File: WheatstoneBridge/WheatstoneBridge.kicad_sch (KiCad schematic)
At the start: 6 parts

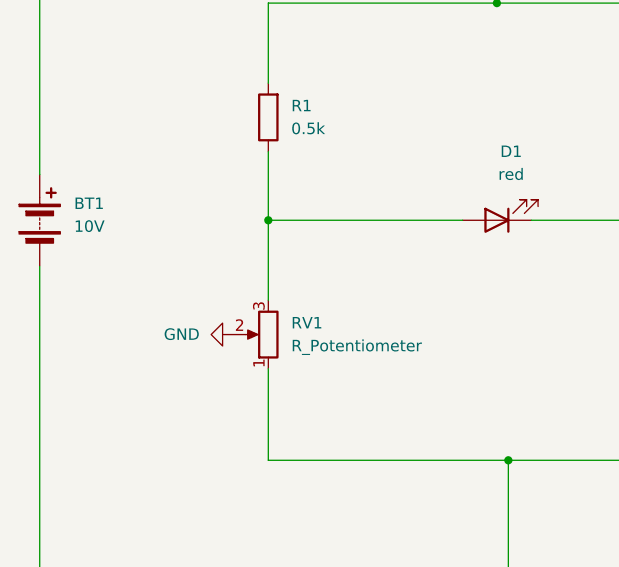
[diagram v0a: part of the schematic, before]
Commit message: Add 4bits adder
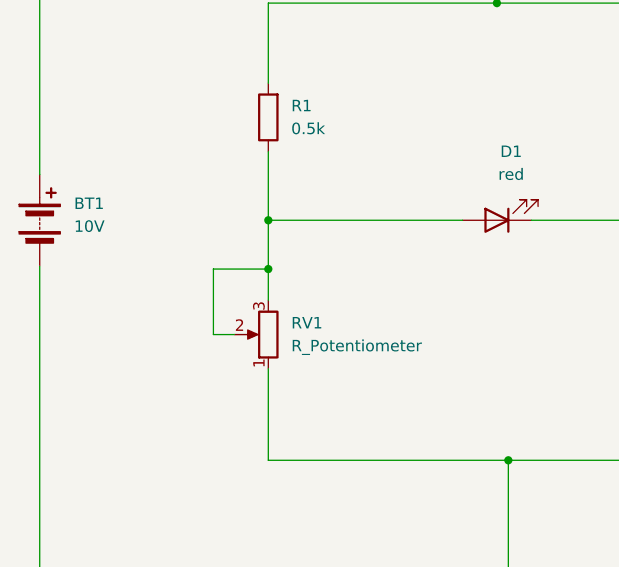
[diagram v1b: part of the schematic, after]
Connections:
- net GND: no longer RV1.2
- net at D1.2 (A), R1.1, RV1.3: now also RV1.2
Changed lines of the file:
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@@
+	)
+	(junction
+		(at 127 105.7479)
+		(diameter 0)
+		(color 0 0 0 0)
 	)
 	(junction
@@
 	(wire
 		(pts
+			(xy 127 105.7479) (xy 127 109.22)
+		)
+		(stroke
+			(width 0)
+			(type default)
+		)
+	)
+	(wire
+		(pts
+			(xy 120.8991 113.03) (xy 120.8991 105.7479)
+		)
+		(stroke
+			(width 0)
+			(type default)
+		)
+	)
+	(wire
+		(pts
+			(xy 123.19 113.03) (xy 120.8991 113.03)
+		)
+		(stroke
+			(width 0)
+			(type default)
+		)
+	)
+	(wire
+		(pts
 			(xy 101.6 105.41) (xy 101.6 139.7)
 		)
@@
 	(wire
 		(pts
-			(xy 127 100.33) (xy 127 109.22)
+			(xy 127 100.33) (xy 127 105.7479)
+		)
+		(stroke
+			(width 0)
+			(type default)
+		)
+	)
+	(wire
+		(pts
+			(xy 120.8991 105.7479) (xy 127 105.7479)
 		)
 		(stroke
@@
 					(unit 1)
 				)
-			)
-		)
-	)
-	(symbol
-		(lib_id "power:GND")
-		(at 123.19 113.03 270)
-		(unit 1)
-		(exclude_from_sim no)
-		(in_bom yes)
-		(on_board yes)
-		(dnp no)
-		(fields_autoplaced yes)
-		(property "Reference" "#PWR03"
-			(at 116.84 113.03 0)
-			(effects
-				(font
-					(size 1.27 1.27)
-				)
-				(hide yes)
-			)
-		)
-		(property "Value" "GND"
-			(at 119.38 113.0299 90)
-			(effects
-				(font
-					(size 1.27 1.27)
-				)
-				(justify right)
-			)
-		)
-		(property "Footprint" ""
-			(at 123.19 113.03 0)
-			(effects
-				(font
-					(size 1.27 1.27)
-				)
-				(hide yes)
-			)
-		)
-		(property "Datasheet" ""
-			(at 123.19 113.03 0)
-			(effects
-				(font
-					(size 1.27 1.27)
-				)
-				(hide yes)
-			)
-		)
-		(property "Description" "Power symbol creates a global label with name \"GND\" , ground"
-			(at 123.19 113.03 0)
-			(effects
-				(font
-					(size 1.27 1.27)
-				)
-				(hide yes)
-			)
-		)
-		(pin "1"
-		)
-		(instances
-			(project "WheatstonBridge"
-				(path "/0611fe71-1d24-40c7-ac54-4fb53423ef94"
-					(reference "#PWR03")
-					(unit 1)
-				)

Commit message: Update wheatstonebridges
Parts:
- removed BT1: 10V, Battery:BatteryHolder_Keystone_1060_1x2032, symbol Device:Battery
- removed D1: red, LED_THT:LED_D5.0mm, symbol Device:LED
- added LED1: D, symbol Simulation_SPICE:D
- added V1: 10, symbol Simulation_SPICE:VDC
- R1: value 0.5k -> 500
- R3: value 0.15k -> 150
- RV1: value R_Potentiometer -> 75
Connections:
- net VCC: now also R2.2, V1.1; no longer R2.1
- net at R1.1, RV1.3: now also LED1.2 (A); no longer RV1.2
- net 0: now reaches R3.1
- net 0: now also RV1.1, RV1.2, V1.2; no longer R2.2
- net GND: no longer names the net of R3.2
- net GND: now also R2.1, LED1.1 (K); no longer RV1.1
